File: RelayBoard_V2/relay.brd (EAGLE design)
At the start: 127 x 85 mm, 30 parts, among them K1 T9AS1D12-5, K2 T9AS1D12-5, T1 2N2222, T2 2N2222, T3 2N2222, T4 2N2222, X1 22-23-2021

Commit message: placed all components on board (not routed)
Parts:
- moved U$7 303.2 mm to (99.1, 24.0)
- moved R7 157.1 mm to (34.3, 87.6)
- moved R8 156.1 mm to (34.3, 82.5)
- moved U$9 147.2 mm to (53.3, 101.6)
- moved U$10 146.6 mm to (35.6, 101.6)
- moved U$11 146.0 mm to (17.8, 101.6)
- moved U$8 121.1 mm to (17.8, 83.8), turned to 270 degrees
- moved R9 119.1 mm to (15.2, 33.0), turned to 270 degrees
- moved T1 78.1 mm to (63.5, 86.4), turned to 270 degrees
- moved R1 58.9 mm to (55.9, 68.6), turned to 270 degrees
- moved R2 58.9 mm to (61.0, 68.6), turned to 270 degrees
- moved R4 50.0 mm to (61.0, 77.5), turned to 270 degrees
- moved X1 44.1 mm to (6.35, 86.4), turned to 90 degrees
- moved T2 42.2 mm to (57.1, 86.4), turned to 270 degrees
- moved R3 39.9 mm to (54.6, 77.5), turned to 270 degrees
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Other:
- board size 127 x 85 mm -> 127 x 114.3 mm

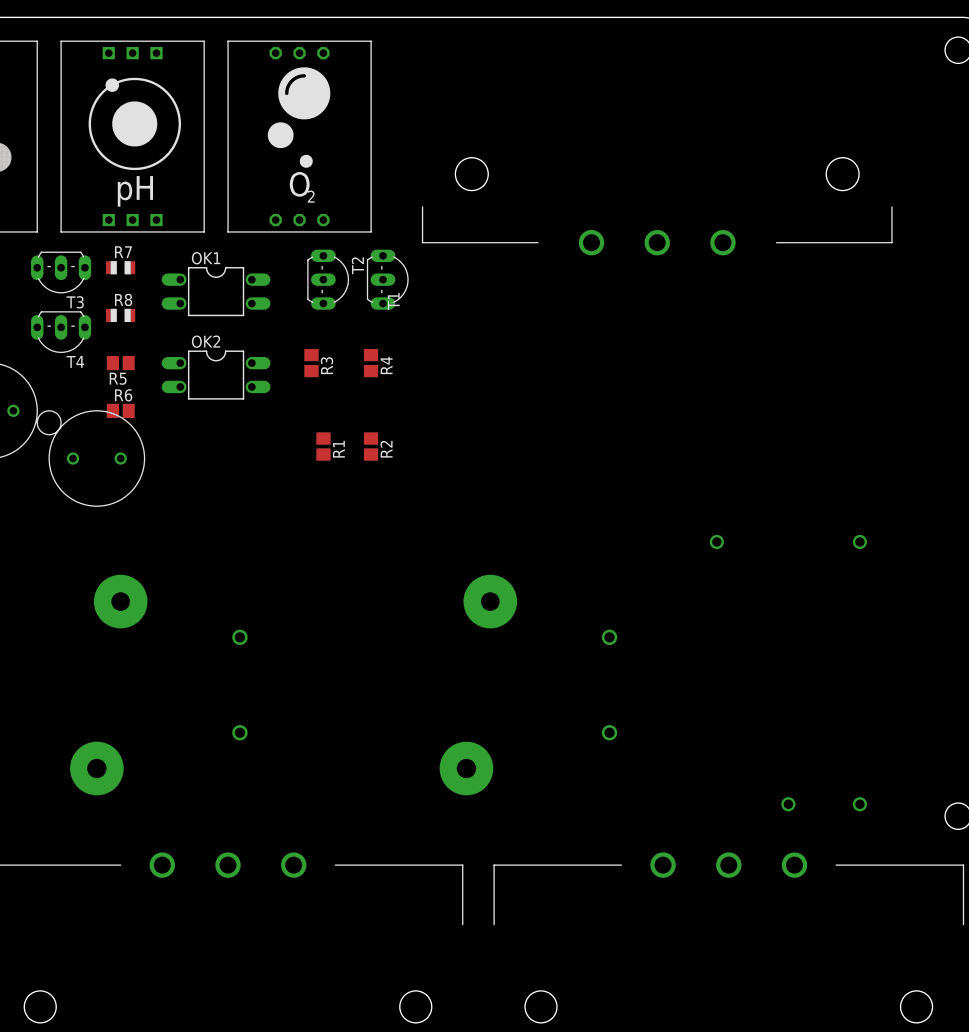
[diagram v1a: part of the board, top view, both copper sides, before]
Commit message: routed ac. 3mm extension on male power receptacle
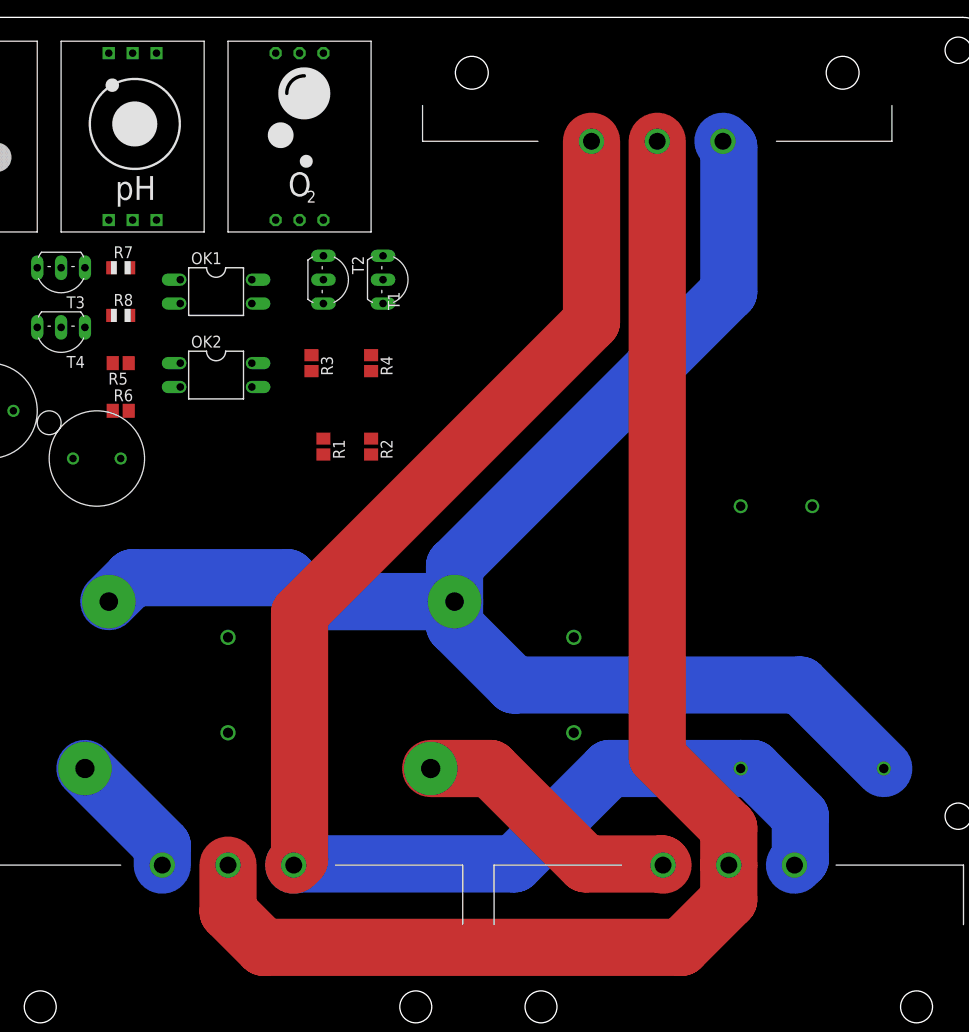
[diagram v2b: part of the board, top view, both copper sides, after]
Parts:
- moved U$17 31.9 mm to (108.0, 62.2), turned to 90 degrees
- moved U$5 10.8 mm to (91.4, 101.1)
- moved K2 3.81 mm to (59.7, 34.3)
- moved K1 1.27 mm to (22.9, 34.3)
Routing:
- net N$20: track 0.00 -> 156.0 mm
- net N$19: track 0.00 -> 154.9 mm
- net PGND: track 0.00 -> 145.9 mm
- net N$17: track 0.00 -> 29.0 mm
- net N$9: track 0.00 -> 13.7 mm
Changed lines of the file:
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@@
 <attribute name="OC_NEWARK" value="97K7059" x="-31.75" y="13.97" size="1.778" layer="27" rot="R270" display="off"/>
 </element>
-<element name="K1" library="BloomWall" package="T9AS1D12-5" value="T9AS1D12-5" x="24.13" y="34.29" smashed="yes" rot="MR270">
-<attribute name="NAME" x="24.13" y="25.4" size="2.0066" layer="26" rot="MR270"/>
-</element>
-<element name="K2" library="BloomWall" package="T9AS1D12-5" value="T9AS1D12-5" x="63.5" y="34.29" smashed="yes" rot="MR270">
-<attribute name="NAME" x="63.5" y="25.4" size="2.0066" layer="26" rot="MR270"/>
+<element name="K1" library="BloomWall" package="T9AS1D12-5" value="T9AS1D12-5" x="22.86" y="34.29" smashed="yes" rot="MR270">
+<attribute name="NAME" x="22.86" y="25.4" size="2.0066" layer="26" rot="MR270"/>
+</element>
+<element name="K2" library="BloomWall" package="T9AS1D12-5" value="T9AS1D12-5" x="59.69" y="34.29" smashed="yes" rot="MR270">
+<attribute name="NAME" x="59.69" y="25.4" size="2.0066" layer="26" rot="MR270"/>
 </element>
 <element name="U$2" library="BloomWall" package="VTB8441BH" value="VTB8441BH" x="20.32" y="72.39"/>
 <element name="U$3" library="BloomWall" package="VTB8441BH" value="VTB8441BH" x="31.75" y="67.31"/>
-<element name="U$17" library="BloomWall" package="RAC02-05SC_ACDCCONVERTER" value="RAC02-05SC_ACDCCONVERTER" x="105.41" y="30.48" rot="R270"/>
+<element name="U$17" library="BloomWall" package="RAC02-05SC_ACDCCONVERTER" value="RAC02-05SC_ACDCCONVERTER" x="107.95" y="62.23" rot="R90"/>
 <element name="X1" library="con-molex" package="22-23-2021" value="22-23-2021" x="6.35" y="86.36" smashed="yes" rot="R90">
 <attribute name="MF" value="MOLEX" x="6.35" y="86.36" size="1.778" layer="27" rot="R90" display="off"/>
@@
 <element name="U$1" library="BloomWall" package="PIN_20X2_NOTFLIPPED" value="PIN_20X2_NOTFLIPPED" x="7.62" y="28.370071875"/>
 <element name="U$4" library="BloomWall" package="9POS_MINI_DIN" value="9POS_MINI_DIN" x="9.652" y="-2.25" rot="R180"/>
-<element name="U$5" library="BloomWall" package="IEC_MALE" value="IEC_MALE" x="91.44" y="90.299996875"/>
 <element name="U$6" library="BloomWall" package="IEC_FEMALE" value="IEC_FEMALE" x="45.72" y="24.000003125"/>
 <element name="U$7" library="BloomWall" package="IEC_FEMALE" value="IEC_FEMALE" x="99.06" y="24.000003125"/>
+<element name="U$5" library="BloomWall" package="IEC_MALE" value="IEC_MALE" x="91.44" y="101.1"/>
 </elements>
 <signals>
@@
 <contactref element="U$3" pad="ANODE"/>
 <wire x1="25.4" y1="81.28" x2="34.29" y2="67.31" width="0" layer="19" extent="1-1"/>
-<wire x1="86.36" y1="38.1" x2="34.29" y2="67.31" width="0" layer="19" extent="1-1"/>
+<wire x1="82.55" y1="38.1" x2="34.29" y2="67.31" width="0" layer="19" extent="1-1"/>
 </signal>
 <signal name="N$18">
@@
 <contactref element="U$2" pad="ANODE"/>
 <wire x1="22.86" y1="72.39" x2="25.4" y2="87.63" width="0" layer="19" extent="1-1"/>
-<wire x1="46.99" y1="38.1" x2="22.86" y2="72.39" width="0" layer="19" extent="1-1"/>
+<wire x1="45.72" y1="38.1" x2="22.86" y2="72.39" width="0" layer="19" extent="1-1"/>
 </signal>
 <signal name="N$32">
@@
 <contactref element="U$17" pad="+VDCOUT"/>
 <contactref element="X1" pad="2"/>
-<wire x1="48.26" y1="86.36" x2="105.41" y2="30.48" width="0" layer="19" extent="1-1"/>
-<wire x1="86.36" y1="48.26" x2="48.26" y2="86.36" width="0" layer="19" extent="1-1"/>
-<wire x1="29.21" y1="67.31" x2="86.36" y2="48.26" width="0" layer="19" extent="1-1"/>
-<wire x1="6.35" y1="87.63" x2="29.21" y2="67.31" width="0" layer="19" extent="1-1"/>
-<wire x1="17.78" y1="72.39" x2="6.35" y2="87.63" width="0" layer="19" extent="1-1"/>
-<wire x1="48.26" y1="77.47" x2="17.78" y2="72.39" width="0" layer="19" extent="1-1"/>
-<wire x1="46.99" y1="48.26" x2="17.78" y2="72.39" width="0" layer="19" extent="1-1"/>
+<wire x1="82.55" y1="48.26" x2="107.95" y2="62.23" width="0" layer="19" extent="1-1"/>
+<wire x1="45.72" y1="48.26" x2="82.55" y2="48.26" width="0" layer="19" extent="1-1"/>
+<wire x1="29.21" y1="67.31" x2="45.72" y2="48.26" width="0" layer="19" extent="1-1"/>
+<wire x1="17.78" y1="72.39" x2="29.21" y2="67.31" width="0" layer="19" extent="1-1"/>
+<wire x1="6.35" y1="87.63" x2="17.78" y2="72.39" width="0" layer="19" extent="1-1"/>
+<wire x1="48.26" y1="77.47" x2="29.21" y2="67.31" width="0" layer="19" extent="1-1"/>
+<wire x1="48.26" y1="86.36" x2="48.26" y2="77.47" width="0" layer="19" extent="1-1"/>
 </signal>
 <signal name="AGND">
@@
 <contactref element="U$17" pad="-VDCOUT"/>
 <contactref element="X1" pad="1"/>
-<wire x1="30.48" y1="81.28" x2="113.03" y2="30.48" width="0" layer="19" extent="1-1"/>
+<wire x1="30.48" y1="81.28" x2="100.33" y2="62.23" width="0" layer="19" extent="1-1"/>
 <wire x1="6.35" y1="85.09" x2="30.48" y2="81.28" width="0" layer="19" extent="1-1"/>
 <wire x1="30.48" y1="87.63" x2="6.35" y2="85.09" width="0" layer="19" extent="1-1"/>
@@
 <contactref element="K1" pad="NO"/>
 <contactref element="U$6" pad="HOT"/>
-<wire x1="38.7199875" y1="24.000003125" x2="31.75" y2="34.29" width="0" layer="19" extent="1-1"/>
+<wire x1="38.7199875" y1="24.000003125" x2="38.7199875" y2="26.0500125" width="6.096" layer="16"/>
+<wire x1="38.7199875" y1="26.0500125" x2="30.48" y2="34.29" width="6.096" layer="16"/>
 </signal>
 <signal name="N$17" class="1">
 <contactref element="K2" pad="NO"/>
 <contactref element="U$7" pad="HOT"/>
-<wire x1="92.0599875" y1="24.000003125" x2="71.12" y2="34.29" width="0" layer="19" extent="1-1"/>
+<wire x1="67.31" y1="34.29" x2="73.66" y2="34.29" width="6.096" layer="1"/>
+<wire x1="73.66" y1="34.29" x2="83.82" y2="24.13" width="6.096" layer="1"/>
+<wire x1="83.82" y1="24.13" x2="91.929990625" y2="24.13" width="6.096" layer="1"/>
+<wire x1="91.929990625" y1="24.13" x2="92.0599875" y2="24.000003125" width="6.096" layer="1"/>
 </signal>
 <signal name="N$19" class="1">
@@
 <contactref element="K1" pad="COM"/>
 <contactref element="U$5" pad="HOT"/>
-<wire x1="34.29" y1="52.07" x2="84.4399875" y2="90.299996875" width="0" layer="19" extent="1-1"/>
-<wire x1="73.66" y1="52.07" x2="34.29" y2="52.07" width="0" layer="19" extent="1-1"/>
-<wire x1="97.79" y1="58.42" x2="73.66" y2="52.07" width="0" layer="19" extent="1-1"/>
+<wire x1="69.85" y1="49.53" x2="69.85" y2="52.07" width="6.096" layer="16"/>
+<wire x1="69.85" y1="49.53" x2="76.2" y2="43.18" width="6.096" layer="16"/>
+<wire x1="76.2" y1="43.18" x2="106.68" y2="43.18" width="6.096" layer="16"/>
+<wire x1="106.68" y1="43.18" x2="115.57" y2="34.29" width="6.096" layer="16"/>
+<wire x1="69.85" y1="52.07" x2="69.85" y2="55.88" width="6.096" layer="16"/>
+<wire x1="99.06" y1="85.09" x2="99.06" y2="100.4800125" width="6.096" layer="16"/>
+<wire x1="99.06" y1="100.4800125" x2="98.4400125" y2="101.1" width="6.096" layer="16"/>
+<wire x1="69.85" y1="55.88" x2="99.06" y2="85.09" width="6.096" layer="16"/>
+<wire x1="69.85" y1="52.07" x2="54.61" y2="52.07" width="6.096" layer="16"/>
+<wire x1="54.61" y1="52.07" x2="52.07" y2="54.61" width="6.096" layer="16"/>
+<wire x1="52.07" y1="54.61" x2="35.56" y2="54.61" width="6.096" layer="16"/>
+<wire x1="35.56" y1="54.61" x2="33.02" y2="52.07" width="6.096" layer="16"/>
 </signal>
 <signal name="N$20" class="1">
 <contactref element="U$17" pad="VACIN(N)"/>
-<contactref element="U$5" pad="NEUTRAL"/>
 <contactref element="U$6" pad="NEUTRAL"/>
 <contactref element="U$7" pad="NEUTRAL"/>
-<wire x1="52.7200125" y1="24.000003125" x2="98.4400125" y2="90.299996875" width="0" layer="19" extent="1-1"/>
-<wire x1="106.0600125" y1="24.000003125" x2="52.7200125" y2="24.000003125" width="0" layer="19" extent="1-1"/>
-<wire x1="113.03" y1="58.42" x2="98.4400125" y2="90.299996875" width="0" layer="19" extent="1-1"/>
+<contactref element="U$5" pad="NEUTRAL"/>
+<wire x1="101.6" y1="34.29" x2="100.33" y2="34.29" width="6.096" layer="16"/>
+<wire x1="101.6" y1="34.29" x2="106.68" y2="29.21" width="6.096" layer="16"/>
+<wire x1="106.68" y1="29.21" x2="106.68" y2="24.619990625" width="6.096" layer="16"/>
+<wire x1="106.68" y1="24.619990625" x2="106.0600125" y2="24.000003125" width="6.096" layer="16"/>
+<wire x1="100.33" y1="34.29" x2="86.36" y2="34.29" width="6.096" layer="16"/>
+<wire x1="86.36" y1="34.29" x2="76.2" y2="24.13" width="6.096" layer="16"/>
+<wire x1="76.2" y1="24.13" x2="52.850009375" y2="24.13" width="6.096" layer="16"/>
+<wire x1="52.850009375" y1="24.13" x2="52.7200125" y2="24.000003125" width="6.096" layer="16"/>
+<wire x1="84.4399875" y1="101.1" x2="84.4399875" y2="81.8999875" width="6.096" layer="1"/>
+<wire x1="84.4399875" y1="81.8999875" x2="53.34" y2="50.8" width="6.096" layer="1"/>
+<wire x1="53.34" y1="50.8" x2="53.34" y2="24.619990625" width="6.096" layer="1"/>
+<wire x1="53.34" y1="24.619990625" x2="52.7200125" y2="24.000003125" width="6.096" layer="1"/>
 </signal>
 <signal name="PGND" class="1">
-<contactref element="U$5" pad="GND"/>
 <contactref element="U$6" pad="GROUND"/>
 <contactref element="U$7" pad="GROUND"/>
-<wire x1="45.72" y1="24.000003125" x2="91.44" y2="90.299996875" width="0" layer="19" extent="1-1"/>
-<wire x1="99.06" y1="24.000003125" x2="45.72" y2="24.000003125" width="0" layer="19" extent="1-1"/>
+<contactref element="U$5" pad="GND"/>
+<wire x1="91.44" y1="101.1" x2="91.44" y2="35.56" width="6.096" layer="1"/>
+<wire x1="91.44" y1="35.56" x2="99.06" y2="27.94" width="6.096" layer="1"/>
+<wire x1="99.06" y1="24.000003125" x2="99.06" y2="27.94" width="6.096" layer="1"/>
+<wire x1="45.72" y1="24.000003125" x2="45.72" y2="19.05" width="6.096" layer="1"/>
+<wire x1="45.72" y1="19.05" x2="49.53" y2="15.24" width="6.096" layer="1"/>
+<wire x1="49.53" y1="15.24" x2="93.98" y2="15.24" width="6.096" layer="1"/>
+<wire x1="93.98" y1="15.24" x2="99.06" y2="20.32" width="6.096" layer="1"/>
+<wire x1="99.06" y1="20.32" x2="99.06" y2="24.000003125" width="6.096" layer="1"/>
 </signal>
 <signal name="N$7">
